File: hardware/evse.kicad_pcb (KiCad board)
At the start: 2 copper layers, 42.5 x 62.5 mm, 85 parts, among them J101 Boot, P101 CON-SENSOR2, P102 Relay, P104 12V/Motor/GP, P105 CP/PP/PE, U101 XMC1100, U102 PEM1-S12-D12-S, U103 MAX14850, U104 ADS1118I, U105 OPA171AIDBV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

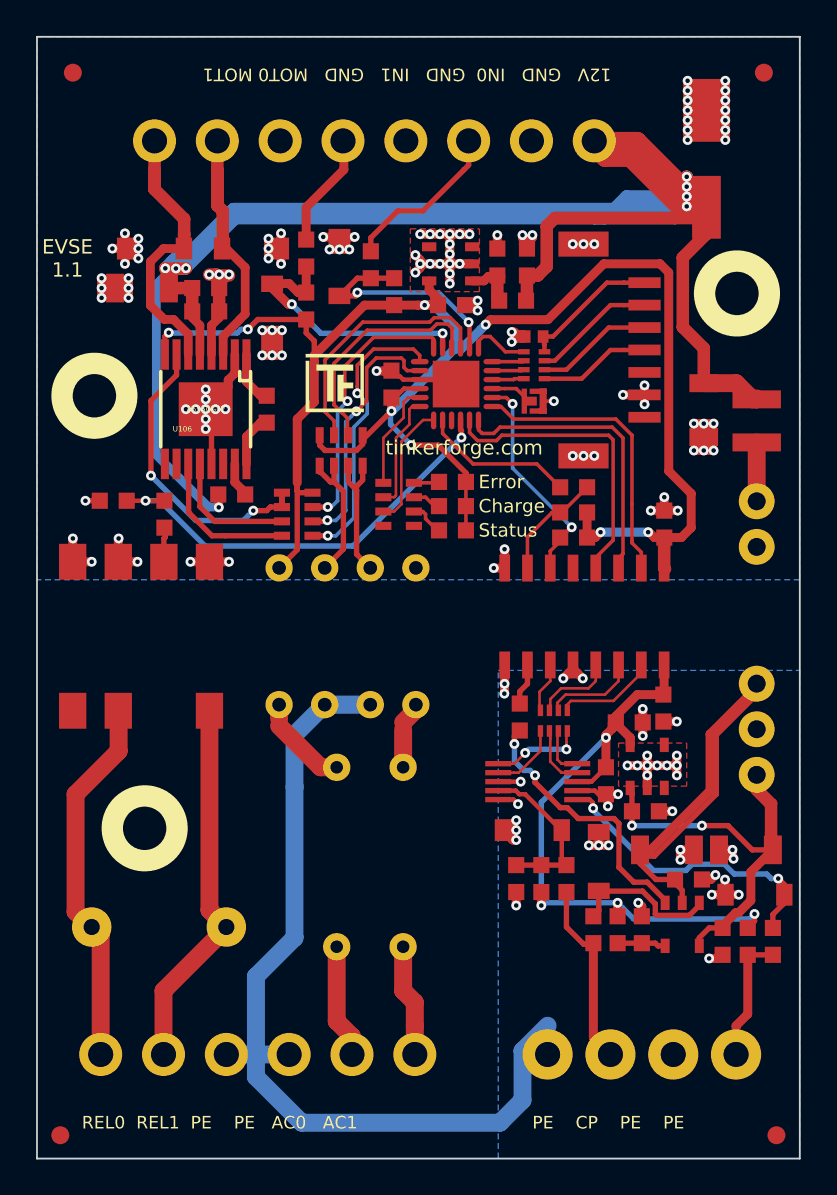
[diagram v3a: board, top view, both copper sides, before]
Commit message: change mounting hole positions
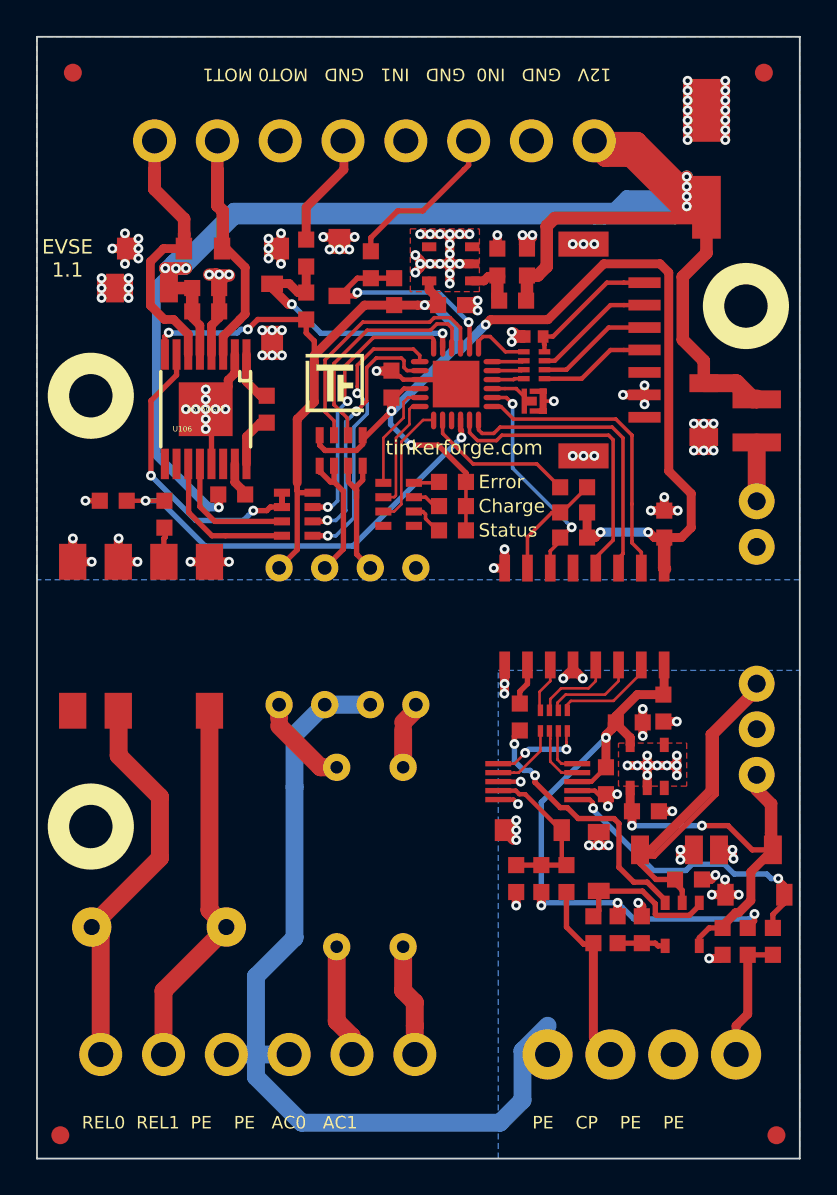
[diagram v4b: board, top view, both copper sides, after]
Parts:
- moved A101 3.00 mm to (142.0, 101.2)
- moved A102 0.86 mm to (178.5, 72.2)
- moved A103 0.20 mm to (142.0, 77.2)
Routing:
- net Net-(P102-Pad1): track 20.8 -> 22.0 mm
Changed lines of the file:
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@@
     (thickness 1.6)
     (drawings 13)
-    (tracks 1091)
+    (tracks 1092)
     (zones 0)
     (modules 85)
@@
   )
   (module kicad-libraries:DRILL_NP (layer F.Cu)
-    (at 145 101.25)
+    (at 142 101.15)
     (fp_text reference A101 (at 0 0) (layer F.SilkS) hide
       (effects (font (size 0.29972 0.29972) (thickness 0.0762)))
@@
   )
   (module kicad-libraries:DRILL_NP (layer F.Cu)
-    (at 178 71.45)
+    (at 178.5 72.15)
     (fp_text reference A102 (at 0 0) (layer F.SilkS) hide
       (effects (font (size 0.29972 0.29972) (thickness 0.0762)))
@@
   )
   (module kicad-libraries:DRILL_NP (layer F.Cu)
-    (at 142.2 77.15)
+    (at 142 77.15)
     (fp_text reference A103 (at 0 0) (layer F.SilkS) hide
       (effects (font (size 0.29972 0.29972) (thickness 0.0762)))
@@
   (segment (start 180.00114 102.45) (end 180.00114 99.85114) (width 0.5) (layer F.Cu) (net 3))
   (segment (start 180.00114 99.85114) (end 179.1 98.95) (width 0.5) (layer F.Cu) (net 3))
-  (segment (start 172.15 100.2) (end 172.15 99) (width 0.3) (layer F.Cu) (net 3))
   (segment (start 172.15 99.35) (end 172.05 99.25) (width 0.3) (layer F.Cu) (net 3))
   (via (at 172.15 101.1) (size 0.55) (drill 0.25) (layers F.Cu B.Cu) (net 3))
-  (segment (start 172.15 100.3) (end 172.15 101.1) (width 0.3) (layer F.Cu) (net 3))
+  (segment (start 172.15 100.3) (end 172.15 101.1) (width 0.5) (layer F.Cu) (net 3))
   (via (at 176.05 101.1) (size 0.55) (drill 0.25) (layers F.Cu B.Cu) (net 3))
   (segment (start 176.05 101.1) (end 177.5 101.1) (width 0.3) (layer F.Cu) (net 3))
@@
   (segment (start 179.8 99.95) (end 179 99.15) (width 0.5) (layer F.Cu) (net 3))
   (segment (start 176.05 101.1) (end 172.15 101.1) (width 0.3) (layer B.Cu) (net 3))
+  (segment (start 172.05 100.1) (end 172.05 98.9) (width 0.5) (layer F.Cu) (net 3))
+  (segment (start 172.15 100.2) (end 172.05 100.1) (width 0.5) (layer F.Cu) (net 3))
   (segment (start 176.3 66.65) (end 176.3 68.15) (width 0.7) (layer F.Cu) (net 4))
   (segment (start 148.07742 74.852) (end 148.07742 73.22742) (width 0.49) (layer F.Cu) (net 4))
@@
   (segment (start 178.85124 77.35) (end 179.1 77.35) (width 1) (layer F.Cu) (net 4))
   (segment (start 179.1 77.35) (end 179.1 77.3) (width 1) (layer F.Cu) (net 4))
-  (segment (start 176.15 74.5) (end 176.15 76.45) (width 0.7) (layer F.Cu) (net 4))
-  (segment (start 174.98 73.33) (end 176.15 74.5) (width 0.7) (layer F.Cu) (net 4))
-  (segment (start 176.3 66.66) (end 176.3 68.13) (width 0.7) (layer F.Cu) (net 4))
-  (segment (start 174.98 69.45) (end 174.98 73.33) (width 0.7) (layer F.Cu) (net 4))
-  (segment (start 176.3 68.13) (end 174.98 69.45) (width 0.7) (layer F.Cu) (net 4))
   (segment (start 149.1 82.65) (end 149.130887 82.680887) (width 0.49) (layer F.Cu) (net 4))
   (segment (start 149.130887 82.980205) (end 149.130887 83.369113) (width 0.49) (layer F.Cu) (net 4))
@@
   (segment (start 172.05 63.9) (end 170.65 63.9) (width 1) (layer F.Cu) (net 4))
   (segment (start 175.75 66.65) (end 174.8 66.65) (width 1) (layer F.Cu) (net 4))
+  (segment (start 176.15 75.2) (end 176.15 76.45) (width 0.7) (layer F.Cu) (net 4))
+  (segment (start 174.98 70.52) (end 174.98 74.03) (width 0.7) (layer F.Cu) (net 4))
+  (segment (start 174.98 74.03) (end 176.15 75.2) (width 0.7) (layer F.Cu) (net 4))
+  (segment (start 176.3 66.66) (end 176.3 69.2) (width 0.7) (layer F.Cu) (net 4))
+  (segment (start 176.3 69.2) (end 174.98 70.52) (width 0.7) (layer F.Cu) (net 4))
   (segment (start 169.1 98.65) (end 169.9 98.65) (width 0.25) (layer F.Cu) (net 5))
   (segment (start 170.4 98.15) (end 170.7 98.15) (width 0.25) (layer F.Cu) (net 5))
@@
   (via (at 171.9 97.75) (size 0.55) (drill 0.25) (layers F.Cu B.Cu) (net 6))
   (segment (start 172.45 97.75) (end 171.9 97.75) (width 0.5) (layer F.Cu) (net 6))
-  (via (at 171.375848 99.35) (size 0.55) (drill 0.25) (layers F.Cu B.Cu) (net 6))
-  (segment (start 170.7 99.35) (end 171.375848 99.35) (width 0.5) (layer F.Cu) (net 6))
   (via (at 172.75 94.6) (size 0.55) (drill 0.25) (layers F.Cu B.Cu) (net 6))
   (segment (start 172.75 95.35) (end 172.75 94.6) (width 0.5) (layer F.Cu) (net 6))
@@
   (via (at 174.65 98.3) (size 0.55) (drill 0.25) (layers F.Cu B.Cu) (net 6))
   (segment (start 174.65 97.75) (end 174.65 98.3) (width 0.5) (layer F.Cu) (net 6))
+  (segment (start 170.7 99.35) (end 171.32599 99.35) (width 0.5) (layer F.Cu) (net 6))
+  (via (at 171.32599 99.35) (size 0.55) (drill 0.25) (layers F.Cu B.Cu) (net 6))
   (segment (start 174.95 104.70107) (end 174.5 104.25107) (width 0.3) (layer F.Cu) (net 7))
   (segment (start 174.95 105.40112) (end 174.95 104.70107) (width 0.3) (layer F.Cu) (net 7))
@@
   (segment (start 155.7 112) (end 156.55006 112.85006) (width 1) (layer F.Cu) (net 17))
   (segment (start 142.54982 107.19982) (end 142.1 106.75) (width 1) (layer F.Cu) (net 18))
-  (segment (start 143.55 96.95) (end 143.55 94.7) (width 1) (layer F.Cu) (net 18))
-  (segment (start 141.15 99.35) (end 143.55 96.95) (width 1) (layer F.Cu) (net 18))
-  (segment (start 141.15 105.9) (end 141.15 99.35) (width 1) (layer F.Cu) (net 18))
-  (segment (start 142.05 106.75) (end 142 106.75) (width 1) (layer F.Cu) (net 18))
-  (segment (start 142 106.75) (end 141.15 105.9) (width 1) (layer F.Cu) (net 18))
   (segment (start 142.54982 107.19982) (end 142.54982 113.89982) (width 1) (layer F.Cu) (net 18))
   (segment (start 142.54982 113.89982) (end 142.55 113.9) (width 1) (layer F.Cu) (net 18))
+  (segment (start 143.55 97.2) (end 143.55 94.7) (width 1) (layer F.Cu) (net 18))
+  (segment (start 145.85 99.5) (end 143.55 97.2) (width 1) (layer F.Cu) (net 18))
+  (segment (start 145.85 102.9) (end 145.85 99.5) (width 1) (layer F.Cu) (net 18))
+  (segment (start 142.05 106.75) (end 142 106.75) (width 1) (layer F.Cu) (net 18))
+  (segment (start 142 106.75) (end 145.85 102.9) (width 1) (layer F.Cu) (net 18))
   (segment (start 166.32754 86.75252) (end 166.32754 85.02246) (width 0.2) (layer F.Cu) (net 19))
   (segment (start 166.32754 85.02246) (end 167.7 83.65) (width 0.2) (layer F.Cu) (net 19))

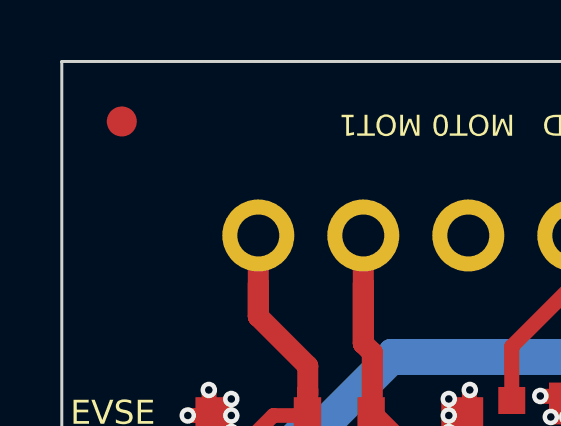
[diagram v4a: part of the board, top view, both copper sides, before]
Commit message: change fiducial positons
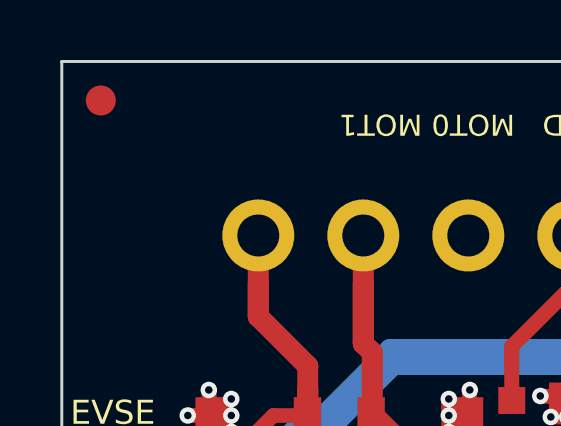
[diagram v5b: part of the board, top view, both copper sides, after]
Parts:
- moved Fiducial_Mark 0.99 mm to (140.3, 58.5)
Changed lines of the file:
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@@
   )
   (module kicad-libraries:Fiducial_Mark (layer F.Cu)
-    (at 141 59.15)
+    (at 140.3 58.45)
     (attr smd)
     (fp_text reference Fiducial_Mark (at 0 0) (layer F.SilkS) hide

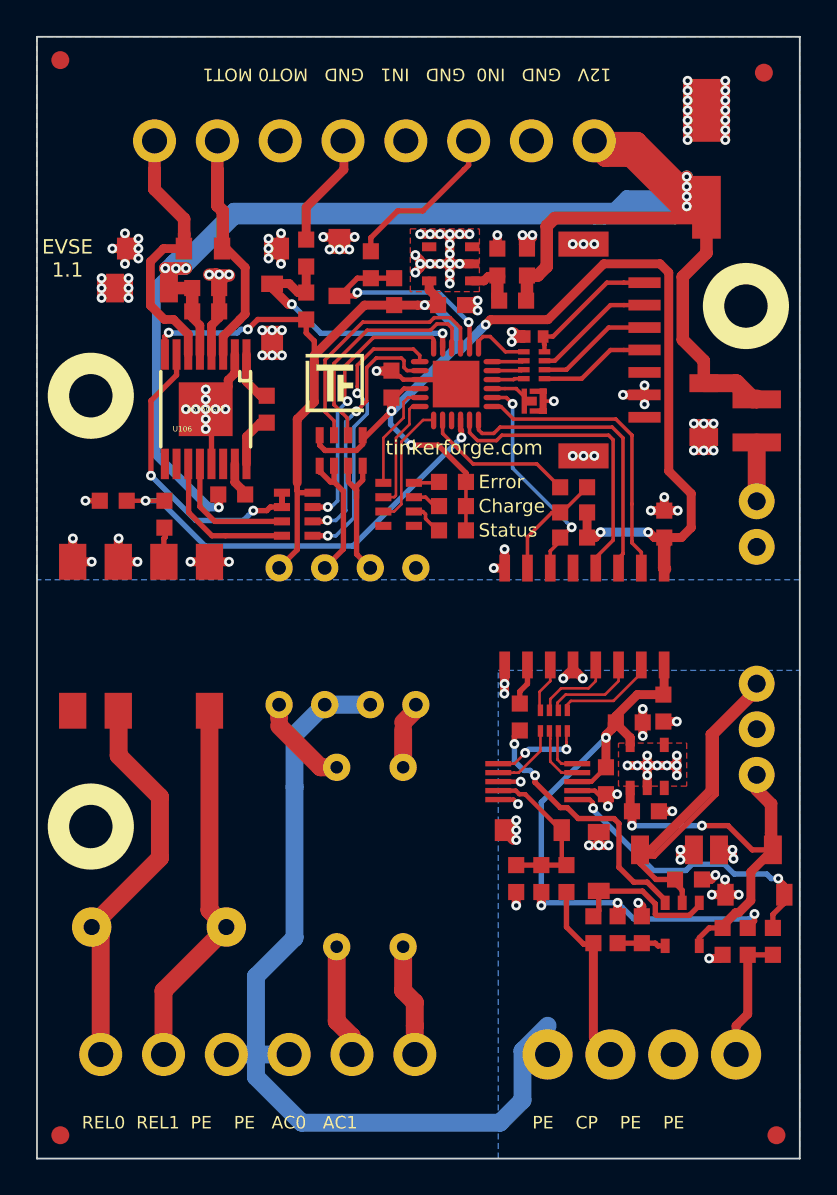
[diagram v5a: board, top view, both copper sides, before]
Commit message: add some artwork, add missing pullup resistors for pwm and cs
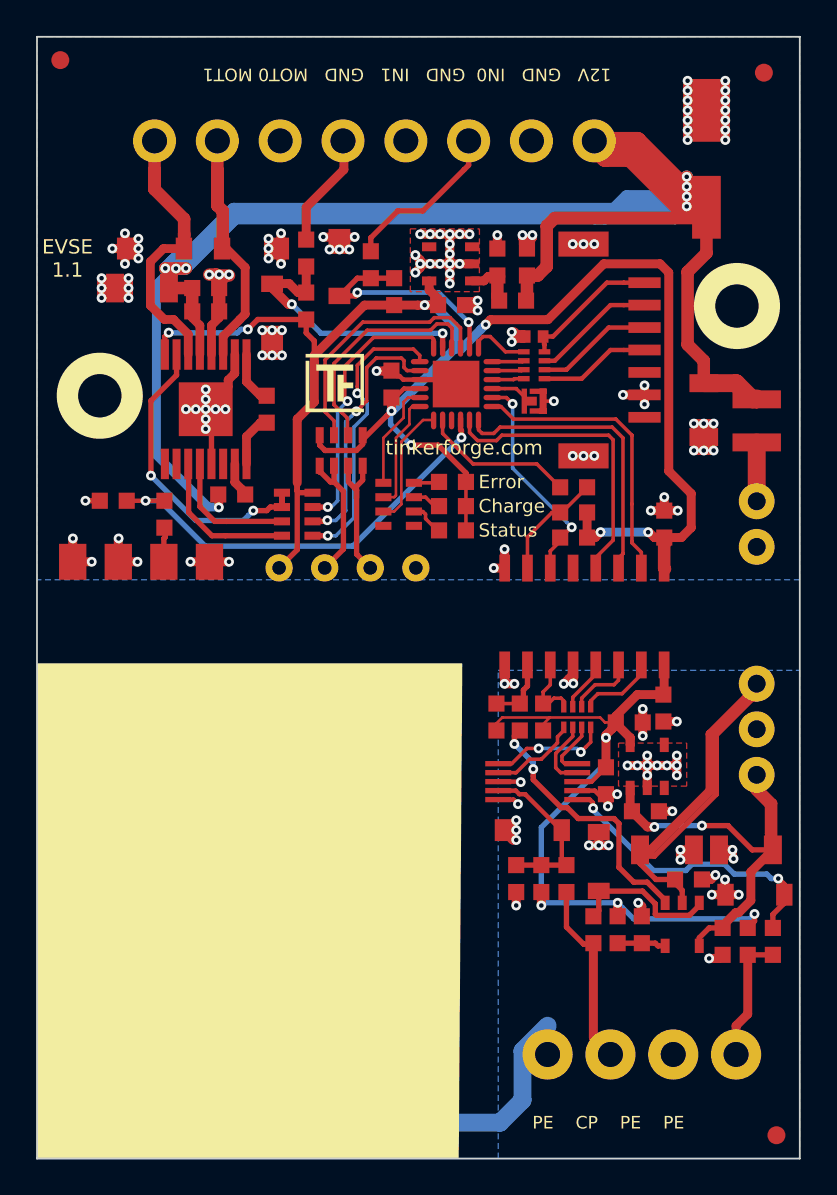
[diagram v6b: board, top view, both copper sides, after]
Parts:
- added R122: 10k, kicad-libraries:R0603F, F.Cu at (167.2, 95.0)
- added R123: 10k, kicad-libraries:R0603F, F.Cu at (164.6, 95.0)
- moved RP103 1.32 mm to (169.1, 95.0)
- moved A101 0.50 mm to (142.5, 101.2)
- moved A102 0.50 mm to (178.0, 72.2)
- moved A103 0.50 mm to (142.5, 77.2)
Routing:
- net VEE: track 36.9 -> 45.1 mm
- net Net-(RP103-Pad3): track 4.55 -> 2.86 mm
- net Net-(RP103-Pad8): track 5.13 -> 6.66 mm
- net Net-(RP103-Pad2): track 5.30 -> 3.79 mm
- net Net-(RP103-Pad1): track 5.72 -> 4.28 mm
- net Net-(R104-Pad2): track 2.28 -> 3.58 mm
- net Net-(R122-Pad2): track 2.85 -> 3.98 mm
- net Net-(RP103-Pad5): track 3.97 -> 5.00 mm
- net Net-(P102-Pad6): track 6.27 -> 5.68 mm
- net Net-(P102-Pad5): track 6.35 -> 5.78 mm
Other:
- board text added: "High Voltage Area"
- board text added: "Remove these on F.Mask"

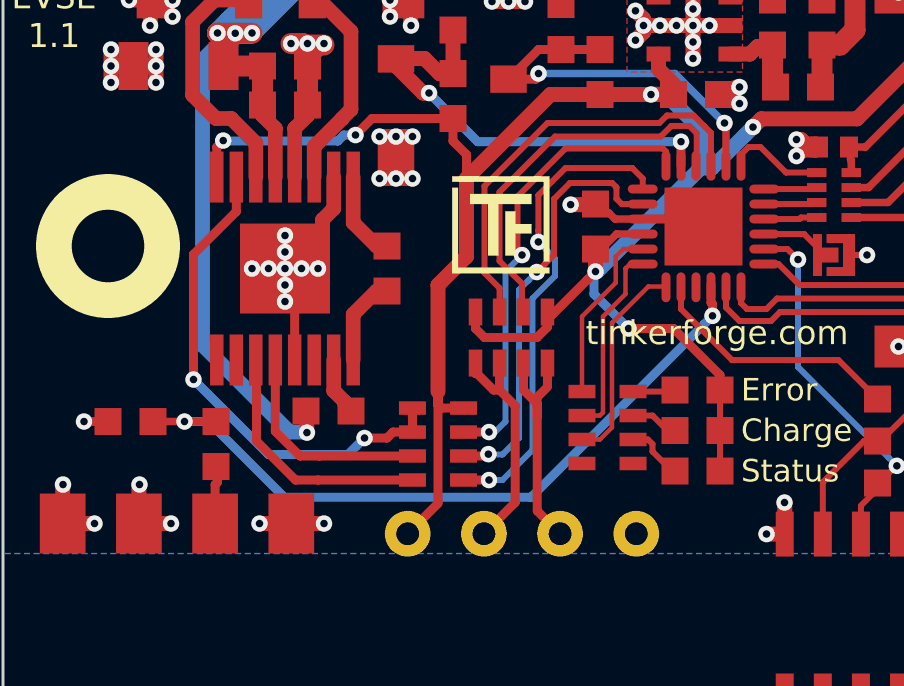
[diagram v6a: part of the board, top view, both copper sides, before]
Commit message: change relay and led pins, fix relay series resistor
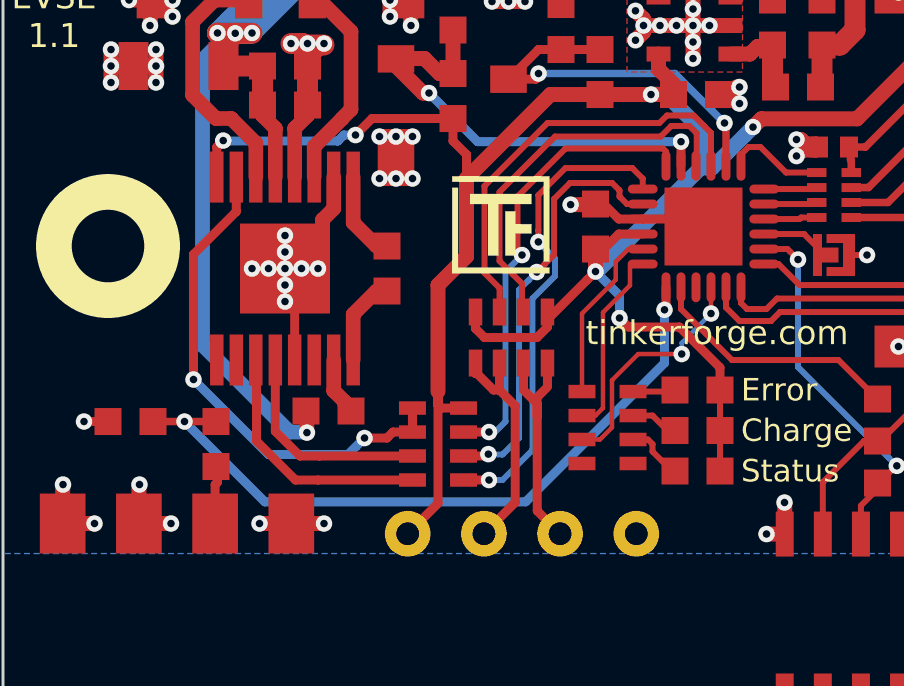
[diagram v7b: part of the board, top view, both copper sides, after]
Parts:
- R114: value 330 -> 150
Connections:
- RP102 pad 2: Net-(RP102-Pad2) -> LED_ERROR
- U101 pad 13: Net-(RP102-Pad2) -> RELAY
- U101 pad 16: RELAY -> LED_ERROR
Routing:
- net LED_ERROR: track 0.00 -> 8.06 mm, vias 0 -> 2
- net Net-(RP102-Pad2): track 6.95 -> 0.00 mm
- net RELAY: track 24.3 -> 23.7 mm
